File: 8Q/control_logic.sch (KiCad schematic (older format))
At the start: 14 parts, among them U181 74LS590, U183 74LS590, U188 28C256, U189 28C256, U192 28C256, U193 28C256, U194 28C256, U195 28C256, U198 28C256, U199 28C256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

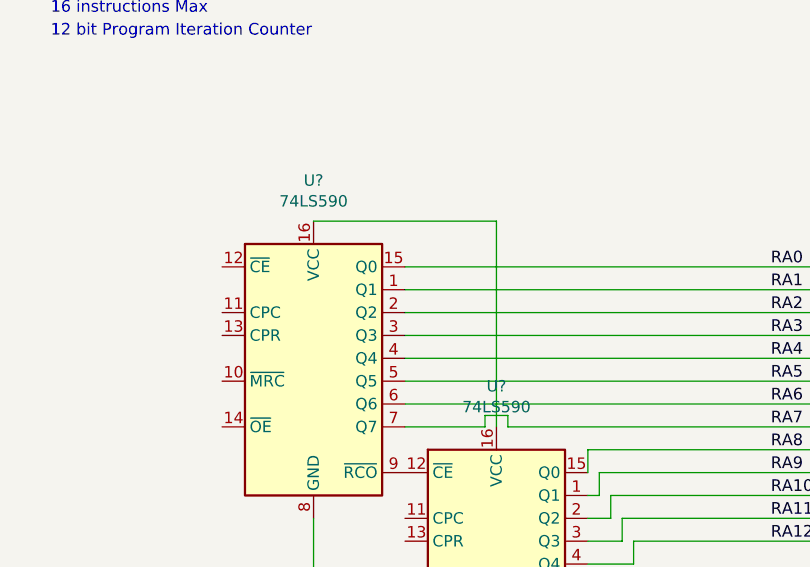
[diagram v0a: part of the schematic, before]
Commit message: modified:   8Q/8Q-cache.lib 	new file:   8Q/8Q-rescue.dcm 	new file:   8Q/8Q-rescue.lib 	modified:   8Q/8Q.kicad_pcb 	modified:   8Q/8Q.sch 	modified:   8Q/8_qp_io.sch 	new file:   8Q/QGates.pretty/CH-Gate.kicad_mod 	new file:   8Q/QGates.pretty/CX-Gate.kicad_mod 	new file:   8Q/QGates.pretty/CY-Gate.kicad_mod 	new file:   8Q/QGates.pretty/CZ-Gate.kicad_mod 	new file:   8Q/QGates.pretty/H-Gate.kicad_mod 	new file:   8Q/QGates.pretty/Measure.kicad_mod 	new file:   8Q/QGates.pretty/Photon-Source.kicad_mod 	new file:   8Q/QGates.pretty/X-Gate.kicad_mod 	new file:   8Q/QGates.pretty/Y-Gate.kicad_mod 	new file:   8Q/QGates.pretty/Z-Gate.kicad_mod 	modified:   8Q/control_logic.sch 	modified:   8Q/cpu.sch 	modified:   8Q/inorder.sch 	modified:   8Q/instruction_bus.sch 	modified:   8Q/output_cache.sch 	modified:   8Q/power.sch 	modified:   8Q/preprocessor.sch 	modified:   8Q/qpower.sch 	modified:   8Q/qpu.sch 	new file:   8Q/sym-lib-table Introduced embedded QSeven module to replace CPU Computer now has support for: * 10Gbps Ethernet * 1xUSB3.0 * 4xUSB2.0 * 1xJTAG * 1xCAN * 1-Wire Bus * 1xSMBus * 1xI2C * External Watchdog * HDMI * LVDS
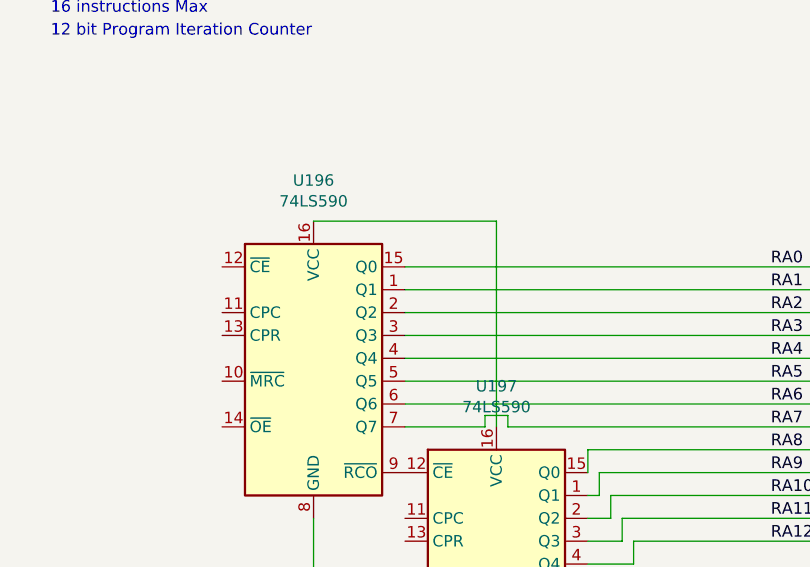
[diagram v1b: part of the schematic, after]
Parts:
- gave numbers to parts that had none: 2
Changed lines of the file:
@@
 EESchema Schematic File Version 4
 LIBS:8Q-cache
+LIBS:Laptop-cache
 EELAYER 26 0
 EELAYER END
 $Descr A1 33110 23386
 encoding utf-8
-Sheet 10 13
+Sheet 10 11
 Title ""
 Date ""
@@
 	5050 5050 5150 5150
 $Comp
-L 74xx:74LS590 U?
+L 74xx:74LS590 U196
 U 1 1 6E7465DD
 P 2650 4350
-F 0 "U?" H 2650 5228 50  0000 C CNN
+F 0 "U196" H 2650 5228 50  0000 C CNN
 F 1 "74LS590" H 2650 5137 50  0000 C CNN
 F 2 "Package_DIP:DIP-16_W7.62mm" H 2650 4400 50  0001 C CNN
@@
 $EndComp
 $Comp
-L 74xx:74LS590 U?
+L 74xx:74LS590 U197
 U 1 1 6E7465E4
 P 3450 5250
-F 0 "U?" H 3450 6128 50  0000 C CNN
+F 0 "U197" H 3450 6128 50  0000 C CNN
 F 1 "74LS590" H 3450 6037 50  0000 C CNN
 F 2 "Package_DIP:DIP-16_W7.62mm" H 3450 5300 50  0001 C CNN
